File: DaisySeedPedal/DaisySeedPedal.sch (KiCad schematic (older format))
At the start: 41 parts, among them J1 Power, J2 GND, J3 Input, J4 Output, SW1 FS1, SW2 FS2, SW3 SW_SPDT, SW4 SW_SPDT, SW5 SW_SPDT, SW6 SW_SPDT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

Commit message: Still placing components
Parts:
- RV1, RV2, RV3, RV4, RV5, RV6: footprint libraries:RK09L1140A65 -> libraries:R_POT
- U2: footprint Package_TO_SOT_THT:TO-92_Inline -> Package_TO_SOT_THT:TO-92_Inline_Wide
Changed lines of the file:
@@
 F 0 "U2" H 6100 5392 50  0000 C CNN
 F 1 "L78L05_TO92" H 6100 5301 50  0000 C CNN
-F 2 "Package_TO_SOT_THT:TO-92_Inline" H 6100 5375 50  0001 C CIN
+F 2 "Package_TO_SOT_THT:TO-92_Inline_Wide" H 6100 5375 50  0001 C CIN
 F 3 "http://www.st.com/content/ccc/resource/technical/document/datasheet/15/55/e5/aa/23/5b/43/fd/CD00000446.pdf/files/CD00000446.pdf/jcr:content/translations/en.CD00000446.pdf" H 6100 5100 50  0001 C CNN
 	1    6100 5150
@@
 F 0 "RV1" V 5643 1300 50  0000 C CNN
 F 1 "R_POT" V 5734 1300 50  0000 C CNN
-F 2 "libraries:RK09L1140A65" H 5850 1300 50  0001 C CNN
+F 2 "libraries:R_POT" H 5850 1300 50  0001 C CNN
 F 3 "~" H 5850 1300 50  0001 C CNN
 	1    5850 1300
@@
 F 0 "RV2" V 6143 1300 50  0000 C CNN
 F 1 "R_POT" V 6234 1300 50  0000 C CNN
-F 2 "libraries:RK09L1140A65" H 6350 1300 50  0001 C CNN
+F 2 "libraries:R_POT" H 6350 1300 50  0001 C CNN
 F 3 "~" H 6350 1300 50  0001 C CNN
 	1    6350 1300
@@
 F 0 "RV3" V 6643 1300 50  0000 C CNN
 F 1 "R_POT" V 6734 1300 50  0000 C CNN
-F 2 "libraries:RK09L1140A65" H 6850 1300 50  0001 C CNN
+F 2 "libraries:R_POT" H 6850 1300 50  0001 C CNN
 F 3 "~" H 6850 1300 50  0001 C CNN
 	1    6850 1300
@@
 F 0 "RV4" V 7143 1300 50  0000 C CNN
 F 1 "R_POT" V 7234 1300 50  0000 C CNN
-F 2 "libraries:RK09L1140A65" H 7350 1300 50  0001 C CNN
+F 2 "libraries:R_POT" H 7350 1300 50  0001 C CNN
 F 3 "~" H 7350 1300 50  0001 C CNN
 	1    7350 1300
@@
 F 0 "RV5" V 7643 1300 50  0000 C CNN
 F 1 "R_POT" V 7734 1300 50  0000 C CNN
-F 2 "libraries:RK09L1140A65" H 7850 1300 50  0001 C CNN
+F 2 "libraries:R_POT" H 7850 1300 50  0001 C CNN
 F 3 "~" H 7850 1300 50  0001 C CNN
 	1    7850 1300
@@
 F 0 "RV6" V 8143 1300 50  0000 C CNN
 F 1 "R_POT" V 8234 1300 50  0000 C CNN
-F 2 "libraries:RK09L1140A65" H 8350 1300 50  0001 C CNN
+F 2 "libraries:R_POT" H 8350 1300 50  0001 C CNN
 F 3 "~" H 8350 1300 50  0001 C CNN
 	1    8350 1300

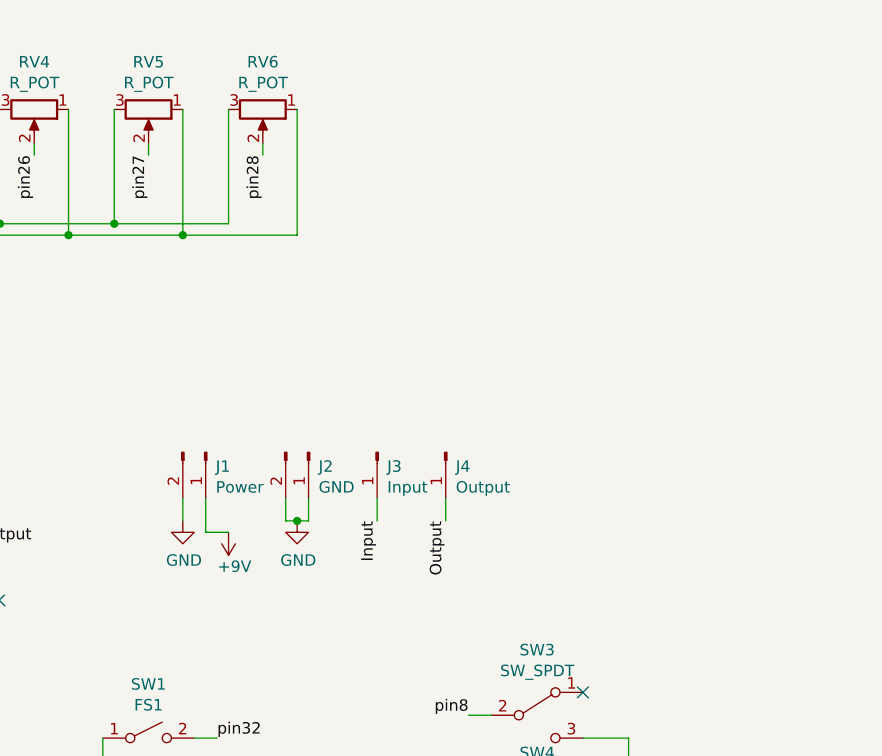
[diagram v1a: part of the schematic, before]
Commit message: Finalized board traces. Now working on silkscreen
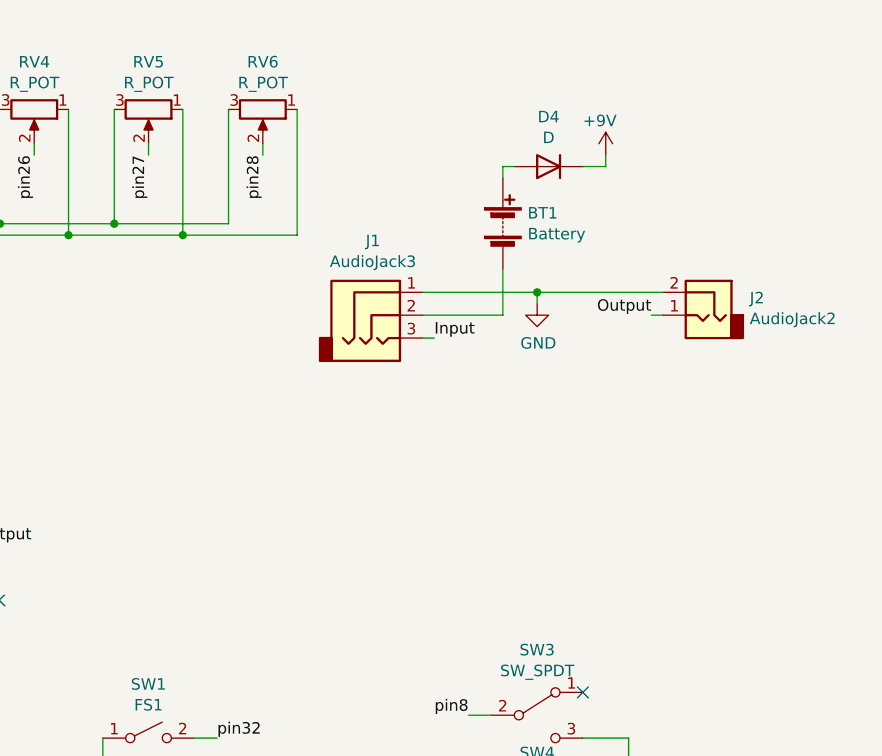
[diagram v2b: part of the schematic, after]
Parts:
- removed J1: Power, Connector_PinSocket_2.54mm:PinSocket_1x02_P2.54mm_Vertical, symbol Connector:Conn_01x02_Male
- removed J2: GND, Connector_PinSocket_2.54mm:PinSocket_1x02_P2.54mm_Vertical, symbol Connector:Conn_01x02_Male
- removed J3: Input, Connector_PinSocket_2.54mm:PinSocket_1x01_P2.54mm_Vertical, symbol Connector:Conn_01x01_Male
- removed J4: Output, Connector_PinSocket_2.54mm:PinSocket_1x01_P2.54mm_Vertical, symbol Connector:Conn_01x01_Male
- added BT1: Battery, Connector_PinSocket_2.54mm:PinSocket_1x02_P2.54mm_Vertical, symbol Device:Battery
- added D4: D, Diode_THT:D_DO-41_SOD81_P10.16mm_Horizontal, symbol Device:D
- added J1: AudioJack3, Connector_PinSocket_2.54mm:PinSocket_1x03_P2.54mm_Vertical, symbol audioJacks:AudioJack3
- added J2: AudioJack2, Connector_PinSocket_2.54mm:PinSocket_1x02_P2.54mm_Vertical, symbol audioJacks:AudioJack2
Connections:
- net +9V: now also D4.1 (K)
- net GND: now also J1.1, J2.2
- net Input: now also J1.3
- net Output: now also J2.1
- new net: BT1.2 (-), J1.2
- new net: BT1.1 (+), D4.2 (A)
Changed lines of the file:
@@
 	8350 1500 8350 1450
-$Comp
-L Connector:Conn_01x02_Male J1
-U 1 1 60CE99D0
-P 8100 2800
-F 0 "J1" V 8162 2844 50  0000 L CNN
-F 1 "Power" V 8253 2844 50  0000 L CNN
-F 2 "Connector_PinSocket_2.54mm:PinSocket_1x02_P2.54mm_Vertical" H 8100 2800 50  0001 C CNN
-F 3 "~" H 8100 2800 50  0001 C CNN
-	1    8100 2800
-	0    1    1    0
-$EndComp
-$Comp
-L Connector:Conn_01x02_Male J2
-U 1 1 60CEA18E
-P 8550 2800
-F 0 "J2" V 8612 2844 50  0000 L CNN
-F 1 "GND" V 8703 2844 50  0000 L CNN
-F 2 "Connector_PinSocket_2.54mm:PinSocket_1x02_P2.54mm_Vertical" H 8550 2800 50  0001 C CNN
-F 3 "~" H 8550 2800 50  0001 C CNN
-	1    8550 2800
-	0    1    1    0
-$EndComp
-$Comp
-L power:GND #PWR06
-U 1 1 60CEA50E
-P 8500 3100
-F 0 "#PWR06" H 8500 2850 50  0001 C CNN
-F 1 "GND" H 8505 2927 50  0000 C CNN
-F 2 "" H 8500 3100 50  0001 C CNN
-F 3 "" H 8500 3100 50  0001 C CNN
-	1    8500 3100
-	1    0    0    -1
-$EndComp
-Wire Wire Line
-	8500 3100 8550 3100
-Wire Wire Line
-	8550 3100 8550 3000
-Wire Wire Line
-	8450 3000 8450 3100
-Wire Wire Line
-	8450 3100 8500 3100
-Connection ~ 8500 3100
-$Comp
-L power:GND #PWR04
-U 1 1 60CF06F9
-P 8000 3100
-F 0 "#PWR04" H 8000 2850 50  0001 C CNN
-F 1 "GND" H 8005 2927 50  0000 C CNN
-F 2 "" H 8000 3100 50  0001 C CNN
-F 3 "" H 8000 3100 50  0001 C CNN
-	1    8000 3100
-	1    0    0    -1
-$EndComp
-Wire Wire Line
-	8000 3100 8000 3000
-$Comp
-L power:+9V #PWR05
-U 1 1 60CF40B4
-P 8200 3150
-F 0 "#PWR05" H 8200 3000 50  0001 C CNN
-F 1 "+9V" H 8100 3300 50  0000 L CNN
-F 2 "" H 8200 3150 50  0001 C CNN
-F 3 "" H 8200 3150 50  0001 C CNN
-	1    8200 3150
-	-1   0    0    1
-$EndComp
-Wire Wire Line
-	8200 3150 8100 3150
-Wire Wire Line
-	8100 3150 8100 3000
-$Comp
-L Connector:Conn_01x01_Male J3
-U 1 1 60CF8F34
-P 8850 2800
-F 0 "J3" V 8912 2844 50  0000 L CNN
-F 1 "Input" V 9003 2844 50  0000 L CNN
-F 2 "Connector_PinSocket_2.54mm:PinSocket_1x01_P2.54mm_Vertical" H 8850 2800 50  0001 C CNN
-F 3 "~" H 8850 2800 50  0001 C CNN
-	1    8850 2800
-	0    1    1    0
-$EndComp
-$Comp
-L Connector:Conn_01x01_Male J4
-U 1 1 60CF9B81
-P 9150 2800
-F 0 "J4" V 9212 2844 50  0000 L CNN
-F 1 "Output" V 9303 2844 50  0000 L CNN
-F 2 "Connector_PinSocket_2.54mm:PinSocket_1x01_P2.54mm_Vertical" H 9150 2800 50  0001 C CNN
-F 3 "~" H 9150 2800 50  0001 C CNN
-	1    9150 2800
-	0    1    1    0
-$EndComp
-Text Label 8850 3100 3    50   ~ 0
-Input
-Wire Wire Line
-	8850 3100 8850 3000
-Text Label 9150 3100 3    50   ~ 0
-Output
-Wire Wire Line
-	9150 3100 9150 3000
 $Comp
 L Switch:SW_SPST SW1
@@
 NoConn ~ 950  6750
 NoConn ~ 950  7150
+$Comp
+L audioJacks:AudioJack2 J2
+U 1 1 60CFF46A
+P 10300 2200
+F 0 "J2" H 10120 2275 50  0000 R CNN
+F 1 "AudioJack2" H 10120 2184 50  0000 R CNN
+F 2 "Connector_PinSocket_2.54mm:PinSocket_1x02_P2.54mm_Vertical" H 10300 2200 50  0001 C CNN
+F 3 "~" H 10300 2200 50  0001 C CNN
+	1    10300 2200
+	-1   0    0    -1
+$EndComp
+$Comp
+L audioJacks:AudioJack3 J1
+U 1 1 60D01170
+P 8850 2200
+F 0 "J1" H 8832 2525 50  0000 C CNN
+F 1 "AudioJack3" H 8832 2434 50  0000 C CNN
+F 2 "Connector_PinSocket_2.54mm:PinSocket_1x03_P2.54mm_Vertical" H 8850 2200 50  0001 C CNN
+F 3 "~" H 8850 2200 50  0001 C CNN
+	1    8850 2200
+	1    0    0    -1
+$EndComp
+$Comp
+L Device:Battery BT1
+U 1 1 60D0B072
+P 9400 1800
+F 0 "BT1" H 9508 1846 50  0000 L CNN
+F 1 "Battery" H 9508 1755 50  0000 L CNN
+F 2 "Connector_PinSocket_2.54mm:PinSocket_1x02_P2.54mm_Vertical" V 9400 1860 50  0001 C CNN
+F 3 "~" V 9400 1860 50  0001 C CNN
+	1    9400 1800
+	1    0    0    -1
+$EndComp
+$Comp
+L Device:D D4
+U 1 1 60D0C848
+P 9600 1550
+F 0 "D4" H 9600 1333 50  0000 C CNN
+F 1 "D" H 9600 1424 50  0000 C CNN
+F 2 "Diode_THT:D_DO-41_SOD81_P10.16mm_Horizontal" H 9600 1550 50  0001 C CNN
+F 3 "~" H 9600 1550 50  0001 C CNN
+	1    9600 1550
+	-1   0    0    1
+$EndComp
+Wire Wire Line
+	9450 1550 9400 1550
+Wire Wire Line
+	9400 1550 9400 1600
+$Comp
+L power:+9V #PWR0112
+U 1 1 60D12C7C
+P 9850 1500
+F 0 "#PWR0112" H 9850 1350 50  0001 C CNN
+F 1 "+9V" H 9750 1650 50  0000 L CNN
+F 2 "" H 9850 1500 50  0001 C CNN
+F 3 "" H 9850 1500 50  0001 C CNN
+	1    9850 1500
+	1    0    0    -1
+$EndComp
+Wire Wire Line
+	9850 1500 9850 1550
+Wire Wire Line
+	9850 1550 9750 1550
+Wire Wire Line
+	9050 2200 9400 2200
+Wire Wire Line
+	9400 2200 9400 2000
+$Comp
+L power:GND #PWR0113
+U 1 1 60D22565
+P 9550 2150
+F 0 "#PWR0113" H 9550 1900 50  0001 C CNN
+F 1 "GND" H 9555 1977 50  0000 C CNN
+F 2 "" H 9550 2150 50  0001 C CNN
+F 3 "" H 9550 2150 50  0001 C CNN
+	1    9550 2150
+	1    0    0    -1
+$EndComp
+Text Label 9100 2300 0    50   ~ 0
+Input
+Wire Wire Line
+	9100 2300 9050 2300
+Text Label 10050 2200 2    50   ~ 0
+Output
+Wire Wire Line
+	9550 2150 9550 2100
+Wire Wire Line
+	9550 2100 9050 2100
+Wire Wire Line
+	9550 2100 10100 2100
+Connection ~ 9550 2100
+Wire Wire Line
+	10050 2200 10100 2200
 $EndSCHEMATC
